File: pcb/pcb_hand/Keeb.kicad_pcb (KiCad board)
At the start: 2 copper layers, 164.4 x 98.5 mm, 70 parts, among them K00 KEYSW, K01 KEYSW, K02 KEYSW, K03 KEYSW, K04 KEYSW, K05 KEYSW, K10 KEYSW, K11 KEYSW, K12 KEYSW, K13 KEYSW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

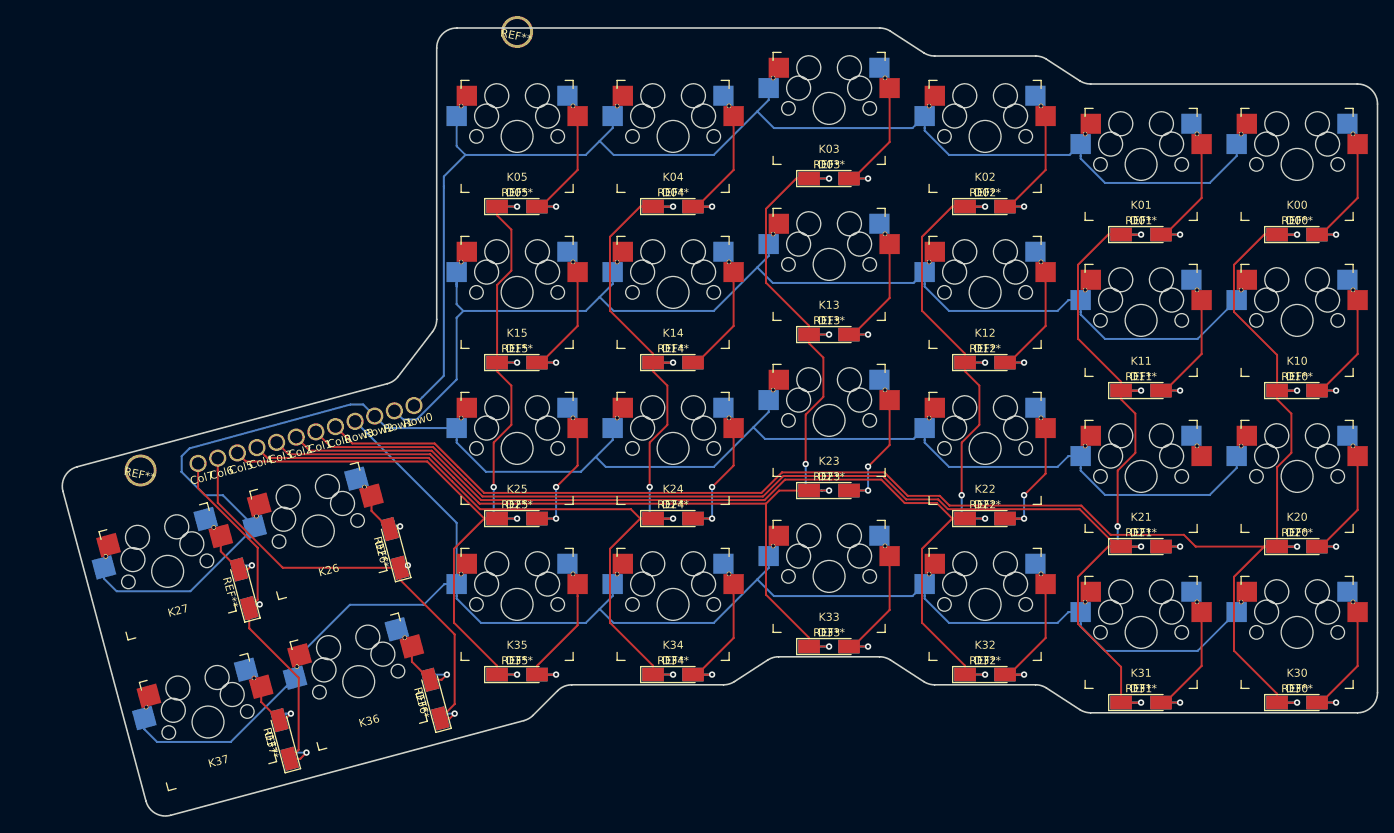
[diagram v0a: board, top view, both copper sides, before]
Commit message: Updated layout to use hirose connectors
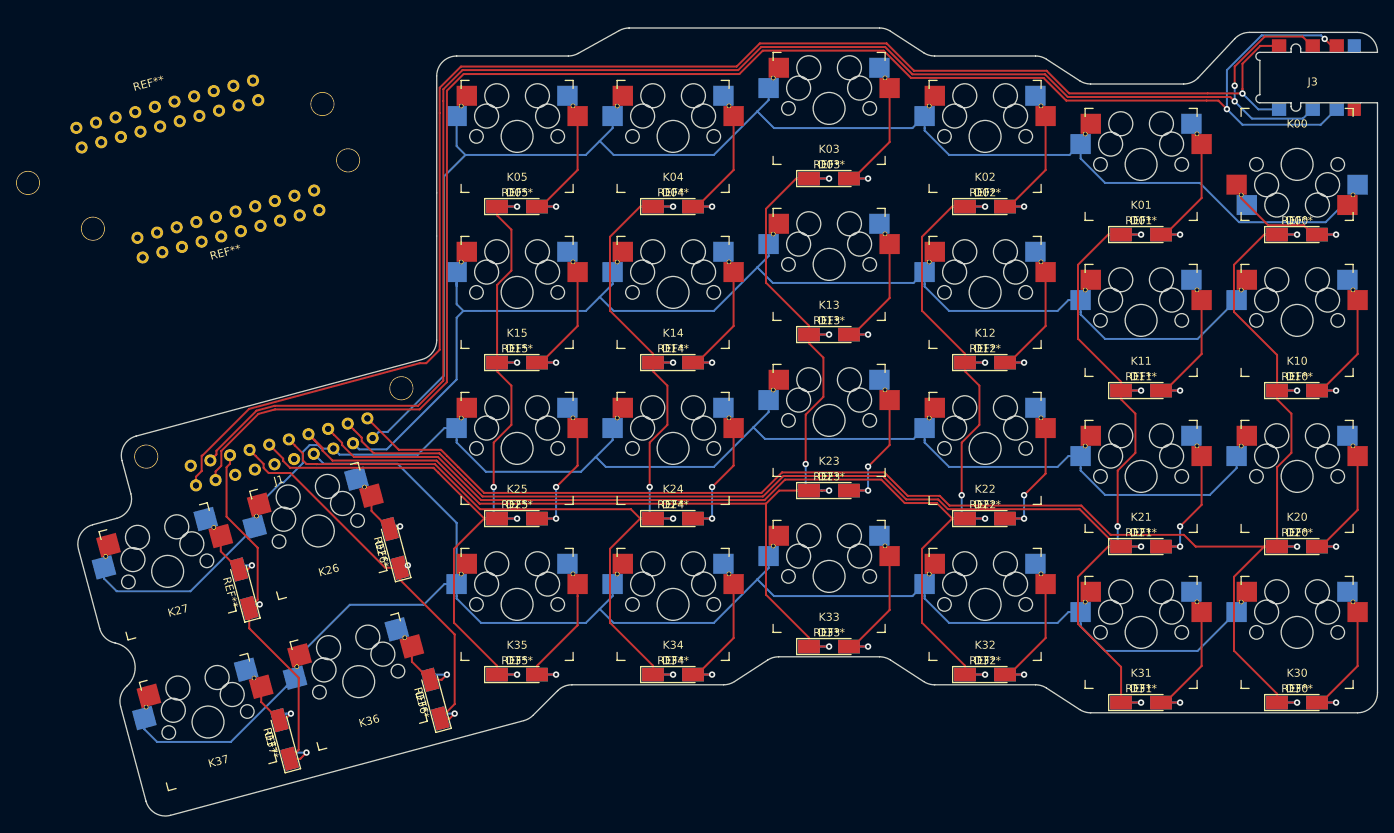
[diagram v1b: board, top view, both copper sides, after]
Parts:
- removed Col0, Col1, Col2, Col3, Col4, Col5, Col6, Col7, Row0, Row1, Row2, Row3: Conn_01x01_Female, SVastaCustomParts:Mill-Max_Pin_Socket_7305-0-15-15-47-27-10-0
- removed the REF** at (320.1, 155.8)
- removed the REF** at (273.1, 210.6)
- added J1: Conn_02x10_Counter_Clockwise, SVastaCustomParts:Backplane_Connector_Hirose_PCN_20pos_Receptacle, F.Cu at (291.7, 212.0)
- added J2: TRRS_SJ1-42514, SVastaCustomParts:3.5mm_Cut_out, B.Cu at (419.6, 161.5)
- added J3: TRRS_SJ1-42514, SVastaCustomParts:3.5mm_Cut_out, F.Cu at (419.6, 161.5)
- added REF**: Backplane_Connector_Hirose_PCN_20pos_Plug, SVastaCustomParts:Backplane_Connector_Hirose_PCN_20pos_Plug, F.Cu at (275.4, 162.4)
- added REF**: Backplane_Connector_Hirose_PCN_20pos_Receptacle, SVastaCustomParts:Backplane_Connector_Hirose_PCN_20pos_Receptacle, F.Cu at (285.0, 183.5)
- turned K00 to 180 degrees
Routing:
- net VCC: track 0.00 -> 211.5 mm, vias 0 -> 2
- net /SDA: track 0.00 -> 201.0 mm, vias 0 -> 2
- net /SCL: track 0.00 -> 190.2 mm, vias 0 -> 1
- net /Row0: track 157.8 -> 198.1 mm
- net /Row3: track 196.5 -> 224.4 mm
- net /Row1: track 143.9 -> 168.9 mm
- net Net-(D21-Pad2): track 4.76 -> 20.2 mm, vias 1 -> 2
- net Net-(D14-Pad2): track 13.7 -> 21.5 mm, vias 0 -> 1
- net /Row2: track 198.5 -> 205.7 mm
- net /Col6: track 60.4 -> 53.9 mm
- net /Col0: track 216.8 -> 213.3 mm
- net /Col2: track 179.5 -> 176.1 mm
- net /Col5: track 122.0 -> 118.6 mm
- net /Col1: track 199.9 -> 196.6 mm
- net Net-(D30-Pad2): track 18.5 -> 21.5 mm
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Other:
- board size 164.4 x 98.5 mm -> 162.5 x 98.5 mm
- board text removed: "Adafruit BLE"
- board text removed: "Battery Holder"
- board text removed: "TRRS"
- board text removed: "USB-C"
